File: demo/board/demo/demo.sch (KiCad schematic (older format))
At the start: 1 part, among them U1 STM32F413CGUx

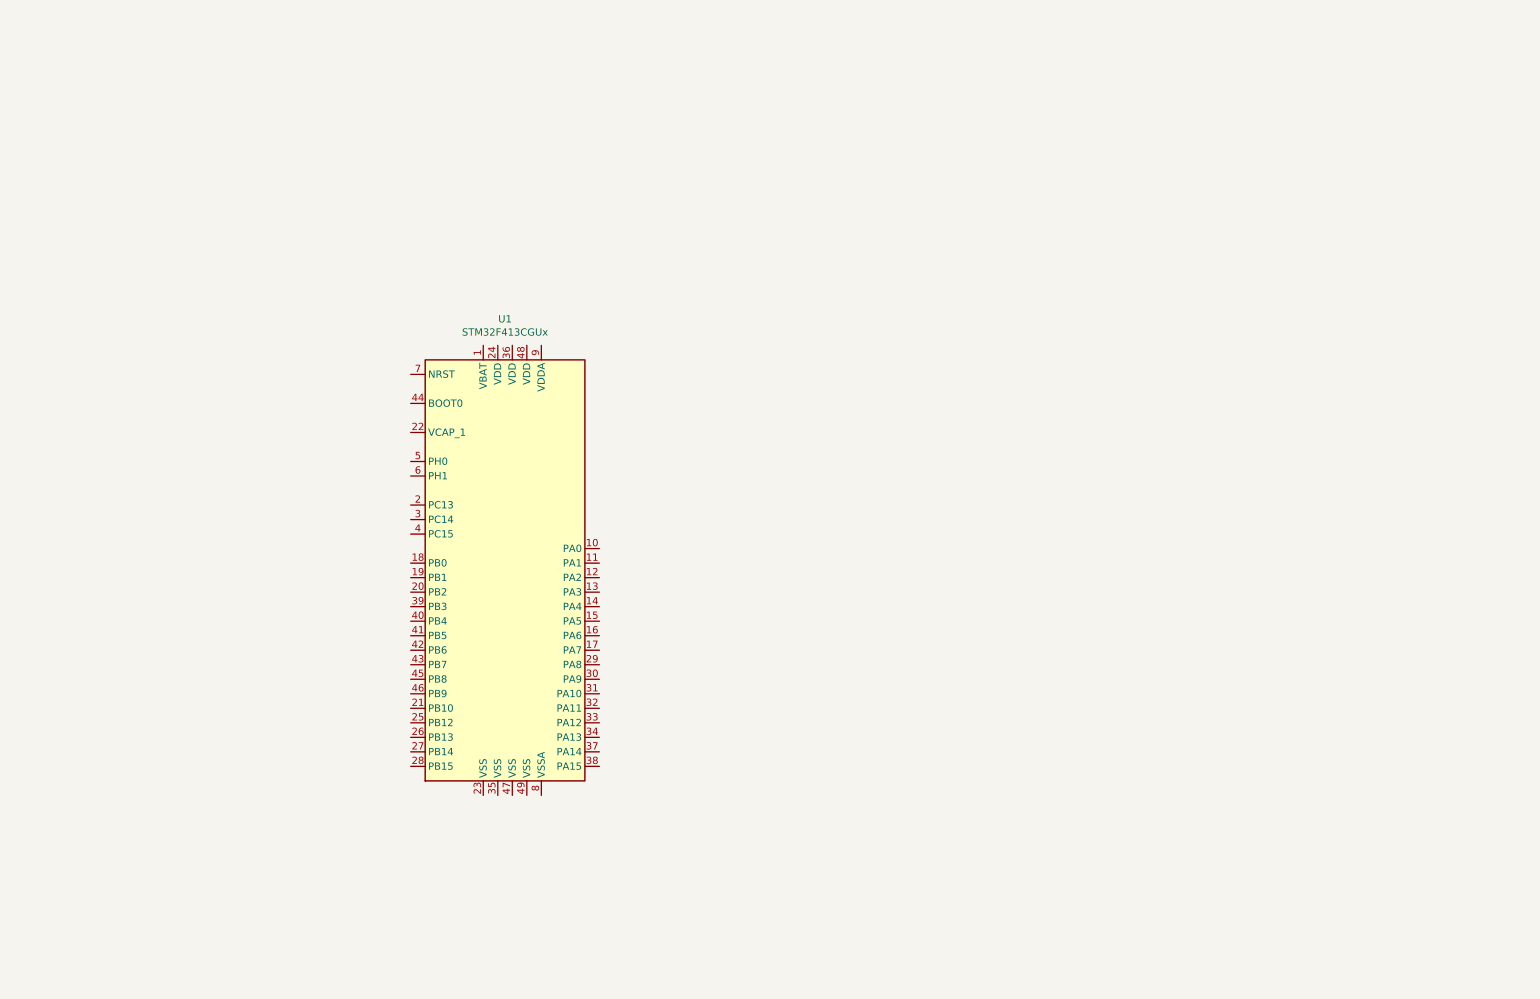
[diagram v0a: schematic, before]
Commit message: initializing project files
- create hardware schematic for dev board (with CAN)
- create CubeIDE project and assign a few pins (empty code)
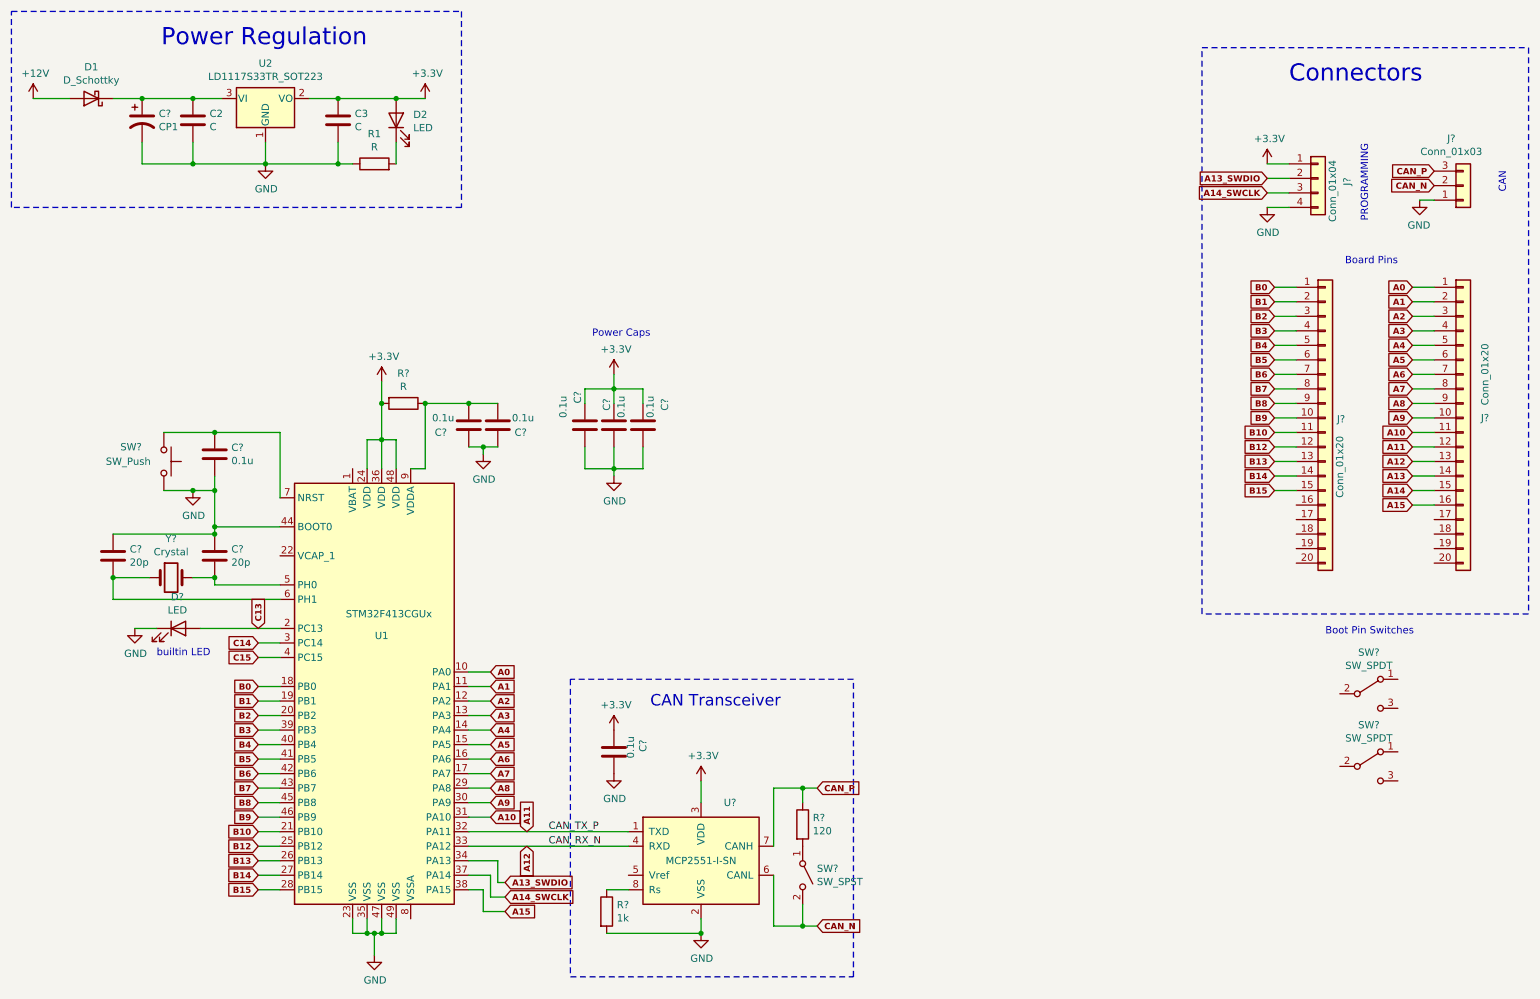
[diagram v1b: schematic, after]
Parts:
- added C2, C3: C, symbol Device:C
- added C? (x7): 0.1u, symbol Device:C
- added C? (x2): 20p, symbol Device:C
- added C?: CP1, symbol Device:CP1
- added D1: D_Schottky, symbol Device:D_Schottky
- added D2, D?: LED, symbol Device:LED
- added J? (x2): Conn_01x20, symbol Connector_Generic:Conn_01x20
- added J?: Conn_01x04, symbol Connector_Generic:Conn_01x04
- added J?: Conn_01x03, symbol Connector_Generic:Conn_01x03
- added R1, R?: R, symbol Device:R
- added R?: 120, symbol Device:R
- added R?: 1k, symbol Device:R
- added SW?: SW_Push, symbol Switch:SW_Push
- added SW? (x2): SW_SPDT, symbol Switch:SW_SPDT
- added SW?: SW_SPST, symbol Switch:SW_SPST
- added U2: LD1117S33TR_SOT223, Package_TO_SOT_SMD:SOT-223-3_TabPin2, symbol Regulator_Linear:LD1117S33TR_SOT223
- added U?: MCP2551-I-SN, Package_SO:SOIC-8_3.9x4.9mm_P1.27mm, symbol Interface_CAN_LIN:MCP2551-I-SN
- added Y?: Crystal, symbol Device:Crystal
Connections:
- net A0: now reaches U1.10 (PA0)
- net A0: now also J?.1 (Pin_1)
- net A1: now reaches U1.11 (PA1)
- net A1: now also J?.2 (Pin_2)
- net A2: now reaches U1.12 (PA2)
- net A2: now also J?.3 (Pin_3)
- net A3: now reaches U1.13 (PA3)
- net A3: now also J?.4 (Pin_4)
- net A4: now reaches U1.14 (PA4)
- net A4: now also J?.5 (Pin_5)
- net A5: now reaches U1.15 (PA5)
- net A5: now also J?.6 (Pin_6)
- net A6: now reaches U1.16 (PA6)
- net A6: now also J?.7 (Pin_7)
- net A7: now reaches U1.17 (PA7)
- net A7: now also J?.8 (Pin_8)
- net B0: now reaches U1.18 (PB0)
- net B0: now also J?.1 (Pin_1)
- net B1: now reaches U1.19 (PB1)
- net B1: now also J?.2 (Pin_2)
- net C13: now reaches U1.2 (PC13)
- net C13: now also D?.2 (A)
- net B2: now reaches U1.20 (PB2)
- net B2: now also J?.3 (Pin_3)
- net B10: now reaches U1.21 (PB10)
- net B10: now also J?.11 (Pin_11)
- net GND: now reaches U1.23 (VSS)
- net GND: now also U1.35 (VSS), U1.44 (BOOT0), U1.47 (VSS), U1.49 (VSS), C2.2, C3.2, C?.1, C?.1, C?.1, C?.1, C?.2, C?.2, C?.2, C?.2, C?.2, C?.2, D?.1 (K), J?.1 (Pin_1), J?.4 (Pin_4), R1.1, R?.2, SW?.2, U2.1 (GND), U?.2 (VSS)
- net +3V3: now reaches U1.24 (VDD)
- net +3V3: now also U1.36 (VDD), U1.48 (VDD), C3.1, C?.1, C?.1, C?.1, C?.1, D2.2 (A), J?.1 (Pin_1), R?.2, U2.2 (VO), U?.3 (VDD)
- net B12: now reaches U1.25 (PB12)
- net B12: now also J?.12 (Pin_12)
- net B13: now reaches U1.26 (PB13)
- net B13: now also J?.13 (Pin_13)
- net B14: now reaches U1.27 (PB14)
- net B14: now also J?.14 (Pin_14)
- net B15: now reaches U1.28 (PB15)
- net B15: now also J?.15 (Pin_15)
- net A8: now reaches U1.29 (PA8)
- net A8: now also J?.9 (Pin_9)
- net C14: now reaches U1.3 (PC14)
- net A9: now reaches U1.30 (PA9)
- net A9: now also J?.10 (Pin_10)
- net A10: now reaches U1.31 (PA10)
- net A10: now also J?.11 (Pin_11)
- net A11: now reaches U1.32 (PA11)
- net A11: now also J?.12 (Pin_12), U?.1 (TXD)
- net A12: now reaches U1.33 (PA12)
- net A12: now also J?.13 (Pin_13), U?.4 (RXD)
- net A13_SWDIO: now reaches U1.34 (PA13)
- net A13_SWDIO: now also J?.2 (Pin_2)
- net A14_SWCLK: now reaches U1.37 (PA14)
- net A14_SWCLK: now also J?.3 (Pin_3)
- net A15: now reaches U1.38 (PA15)
- net A15: now also J?.16 (Pin_16)
- net B3: now reaches U1.39 (PB3)
- net B3: now also J?.4 (Pin_4)
- net C15: now reaches U1.4 (PC15)
- net B4: now reaches U1.40 (PB4)
- net B4: now also J?.5 (Pin_5)
- net B5: now reaches U1.41 (PB5)
- net B5: now also J?.6 (Pin_6)
- net B6: now reaches U1.42 (PB6)
- net B6: now also J?.7 (Pin_7)
- net B7: now reaches U1.43 (PB7)
- net B7: now also J?.8 (Pin_8)
- net B8: now reaches U1.45 (PB8)
- net B8: now also J?.9 (Pin_9)
- net B9: now reaches U1.46 (PB9)
- net B9: now also J?.10 (Pin_10)
- net at U1.5 (PH0): now also C?.2, Y?.2
- net at U1.6 (PH1): now also C?.2, Y?.1
- net at U1.7 (NRST): now also C?.1, SW?.1
- net at U1.9 (VDDA): now also C?.2, C?.2, R?.1
- new net: C2.1, C?.1, D1.1 (K), U2.3 (VI)
- new net: D2.1 (K), R1.2
- new net: R?.1, U?.8 (Rs)
- new net: R?.2, SW?.1 (A)
- new net +12V: D1.2 (A)
- new net A13: J?.14 (Pin_14)
- new net A14: J?.15 (Pin_15)
- new net CAN_N: J?.2 (Pin_2), SW?.2 (B), U?.6 (CANL)
- new net CAN_P: J?.3 (Pin_3), R?.1, U?.7 (CANH)
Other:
- note added: "Board Pins"
- note added: "Boot Pin Switches"
- note added: "CAN"
- note added: "CAN Transceiver"
- note added: "Connectors"
- note added: "PROGRAMMING"
- note added: "Power Caps"
- note added: "Power Regulation"
- note added: "builtin LED"
- moved on the sheet: U1
